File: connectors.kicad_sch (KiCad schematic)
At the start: 10 parts, among them J1 USB-C_DX07S024JJ2, J2 PCIe_x4_Conn_EdgeMount, J3 Molex_Nano-Fit-1053xx_xx02-ho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

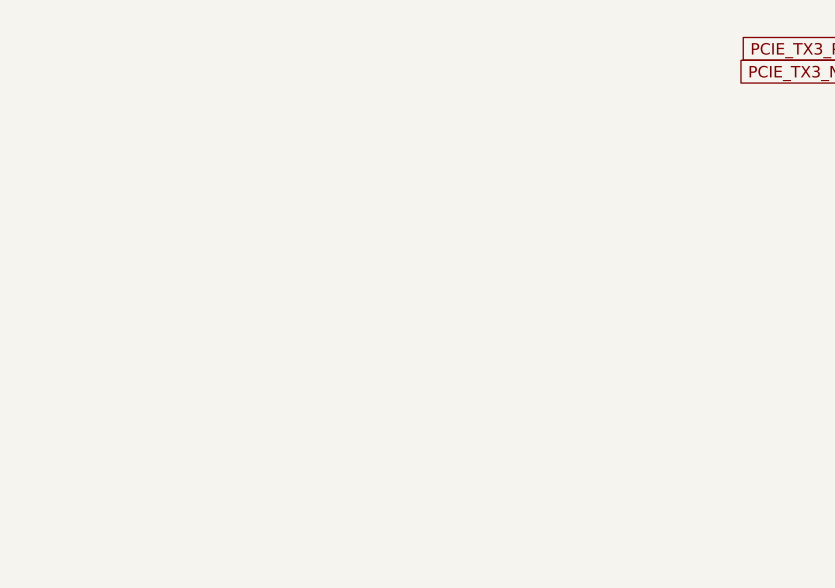
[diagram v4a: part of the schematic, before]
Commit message: Fixed all DRC errors and warnings, finished designators' placement
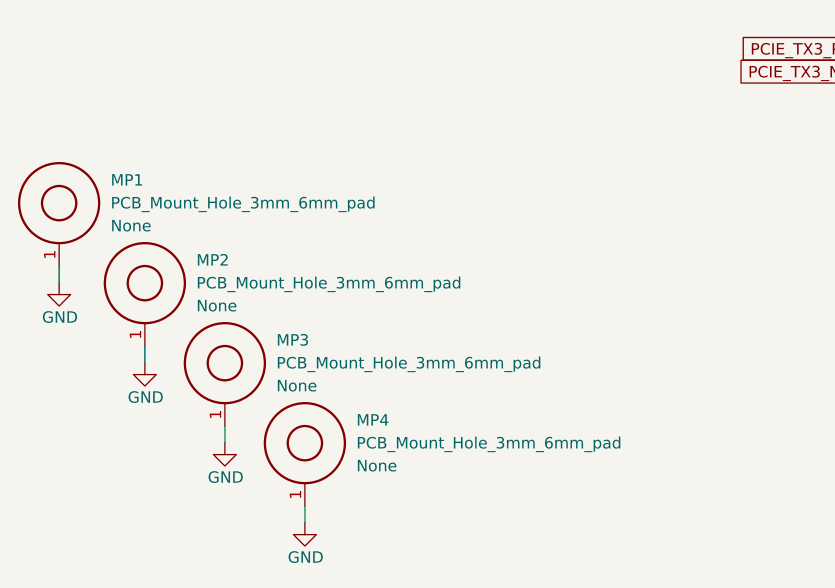
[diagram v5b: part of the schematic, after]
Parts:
- added MP1, MP2, MP3, MP4: PCB_Mount_Hole_3mm_6mm_pad, antmicro-footprints:mounting-hole-3.2mm, symbol antmicroMechanicalParts:PCB_Mount_Hole_3mm_6mm_pad
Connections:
- net GND: now also MP1.1, MP2.1, MP3.1, MP4.1
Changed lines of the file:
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@@
+    (stroke (width 0) (type default) (color 0 0 0 0))
+  )
+  (wire (pts (xy 62.865 383.54) (xy 62.865 385.445))
     (stroke (width 0) (type default) (color 0 0 0 0))
   )
@@
     (stroke (width 0) (type default) (color 0 0 0 0))
   )
+  (wire (pts (xy 45.085 365.76) (xy 45.085 367.665))
+    (stroke (width 0) (type default) (color 0 0 0 0))
+  )
   (wire (pts (xy 161.29 72.39) (xy 170.815 72.39))
     (stroke (width 0) (type default) (color 0 0 0 0))
@@
     (stroke (width 0) (type default) (color 0 0 0 0))
   )
+  (wire (pts (xy 35.56 356.87) (xy 35.56 358.775))
+    (stroke (width 0) (type default) (color 0 0 0 0))
+  )
   (wire (pts (xy 169.545 269.24) (xy 167.64 269.24))
     (stroke (width 0) (type default) (color 0 0 0 0))
@@
   )
   (wire (pts (xy 123.825 281.94) (xy 128.27 281.94))
+    (stroke (width 0) (type default) (color 0 0 0 0))
+  )
+  (wire (pts (xy 53.975 374.65) (xy 53.975 376.555))
     (stroke (width 0) (type default) (color 0 0 0 0))
   )
@@
     )
     (property "Datasheet" "" (id 3) (at 146.685 128.27 0)
+      (effects (font (size 1.27 1.27)) hide)
+    )
+    (pin "1")
+  )
+  (symbol (lib_id "power:GND") (at 53.975 376.555 0) (unit 1)
+    (in_bom yes) (on_board yes)
+    (property "Reference" "#PWR0162" (id 0) (at 53.975 382.905 0)
+      (effects (font (size 1.27 1.27)) hide)
+    )
+    (property "Value" "GND" (id 1) (at 52.07 380.365 0)
+      (effects (font (size 1.27 1.27)) (justify left))
+    )
+    (property "Footprint" "" (id 2) (at 53.975 376.555 0)
+      (effects (font (size 1.27 1.27)) hide)
+    )
+    (property "Datasheet" "" (id 3) (at 53.975 376.555 0)
       (effects (font (size 1.27 1.27)) hide)
     )
@@
     (pin "1")
   )
+  (symbol (lib_id "antmicroMechanicalParts:PCB_Mount_Hole_3mm_6mm_pad") (at 45.085 365.76 90) (unit 1)
+    (in_bom yes) (on_board yes) (fields_autoplaced)
+    (property "Reference" "MP2" (id 0) (at 50.8 356.2349 90)
+      (effects (font (size 1.27 1.27) (thickness 0.15)) (justify right))
+    )
+    (property "Value" "PCB_Mount_Hole_3mm_6mm_pad" (id 1) (at 50.8 358.7749 90)
+      (effects (font (size 1.27 1.27) (thickness 0.15)) (justify right))
+    )
+    (property "Footprint" "antmicro-footprints:mounting-hole-3.2mm" (id 2) (at 52.705 345.44 0)
+      (effects (font (size 1.27 1.27) (thickness 0.15)) (justify left bottom) hide)
+    )
+    (property "Datasheet" "" (id 3) (at 55.245 345.44 0)
+      (effects (font (size 1.27 1.27) (thickness 0.15)) (justify left bottom) hide)
+    )
+    (property "Author" "Antmicro" (id 4) (at 57.785 345.44 0)
+      (effects (font (size 1.27 1.27) (thickness 0.15)) (justify left bottom) hide)
+    )
+    (property "License" "Apache-2.0" (id 5) (at 60.325 345.44 0)
+      (effects (font (size 1.27 1.27) (thickness 0.15)) (justify left bottom) hide)
+    )
+    (property "Manufacturer" "None" (id 6) (at 50.8 361.3149 90)
+      (effects (font (size 1.27 1.27)) (justify right))
+    )
+    (pin "1")
+  )
   (symbol (lib_id "power:GND") (at 181.61 271.145 0) (unit 1)
     (in_bom yes) (on_board yes)
@@
     (pin "1")
   )
+  (symbol (lib_id "power:GND") (at 45.085 367.665 0) (unit 1)
+    (in_bom yes) (on_board yes)
+    (property "Reference" "#PWR0159" (id 0) (at 45.085 374.015 0)
+      (effects (font (size 1.27 1.27)) hide)
+    )
+    (property "Value" "GND" (id 1) (at 43.18 371.475 0)
+      (effects (font (size 1.27 1.27)) (justify left))
+    )
+    (property "Footprint" "" (id 2) (at 45.085 367.665 0)
+      (effects (font (size 1.27 1.27)) hide)
+    )
+    (property "Datasheet" "" (id 3) (at 45.085 367.665 0)
+      (effects (font (size 1.27 1.27)) hide)
+    )
+    (pin "1")
+  )
+  (symbol (lib_id "power:GND") (at 62.865 385.445 0) (unit 1)
+    (in_bom yes) (on_board yes)
+    (property "Reference" "#PWR0161" (id 0) (at 62.865 391.795 0)
+      (effects (font (size 1.27 1.27)) hide)
+    )
+    (property "Value" "GND" (id 1) (at 60.96 389.255 0)
+      (effects (font (size 1.27 1.27)) (justify left))
+    )
+    (property "Footprint" "" (id 2) (at 62.865 385.445 0)
+      (effects (font (size 1.27 1.27)) hide)
+    )
+    (property "Datasheet" "" (id 3) (at 62.865 385.445 0)
+      (effects (font (size 1.27 1.27)) hide)
+    )
+    (pin "1")
+  )
+  (symbol (lib_id "power:GND") (at 35.56 358.775 0) (unit 1)
+    (in_bom yes) (on_board yes)
+    (property "Reference" "#PWR0160" (id 0) (at 35.56 365.125 0)
+      (effects (font (size 1.27 1.27)) hide)
+    )
+    (property "Value" "GND" (id 1) (at 33.655 362.585 0)
+      (effects (font (size 1.27 1.27)) (justify left))
+    )
+    (property "Footprint" "" (id 2) (at 35.56 358.775 0)
+      (effects (font (size 1.27 1.27)) hide)
+    )
+    (property "Datasheet" "" (id 3) (at 35.56 358.775 0)
+      (effects (font (size 1.27 1.27)) hide)
+    )
+    (pin "1")
+  )
+  (symbol (lib_id "antmicroMechanicalParts:PCB_Mount_Hole_3mm_6mm_pad") (at 62.865 383.54 90) (unit 1)
+    (in_bom yes) (on_board yes) (fields_autoplaced)
+    (property "Reference" "MP4" (id 0) (at 68.58 374.0149 90)
+      (effects (font (size 1.27 1.27) (thickness 0.15)) (justify right))
+    )
+    (property "Value" "PCB_Mount_Hole_3mm_6mm_pad" (id 1) (at 68.58 376.5549 90)
+      (effects (font (size 1.27 1.27) (thickness 0.15)) (justify right))
+    )
+    (property "Footprint" "antmicro-footprints:mounting-hole-3.2mm" (id 2) (at 70.485 363.22 0)
+      (effects (font (size 1.27 1.27) (thickness 0.15)) (justify left bottom) hide)
+    )
+    (property "Datasheet" "" (id 3) (at 73.025 363.22 0)
+      (effects (font (size 1.27 1.27) (thickness 0.15)) (justify left bottom) hide)
+    )
+    (property "Author" "Antmicro" (id 4) (at 75.565 363.22 0)
+      (effects (font (size 1.27 1.27) (thickness 0.15)) (justify left bottom) hide)
+    )
+    (property "License" "Apache-2.0" (id 5) (at 78.105 363.22 0)
+      (effects (font (size 1.27 1.27) (thickness 0.15)) (justify left bottom) hide)
+    )
+    (property "Manufacturer" "None" (id 6) (at 68.58 379.0949 90)
+      (effects (font (size 1.27 1.27)) (justify right))
+    )
+    (pin "1")
+  )
   (symbol (lib_id "power:GND") (at 153.035 195.58 0) (unit 1)
     (in_bom yes) (on_board yes)
@@
     (property "Datasheet" "" (id 3) (at 140.335 128.27 0)
       (effects (font (size 1.27 1.27)) hide)
+    )
+    (pin "1")
+  )
+  (symbol (lib_id "antmicroMechanicalParts:PCB_Mount_Hole_3mm_6mm_pad") (at 35.56 356.87 90) (unit 1)
+    (in_bom yes) (on_board yes) (fields_autoplaced)
+    (property "Reference" "MP1" (id 0) (at 41.275 347.3449 90)
+      (effects (font (size 1.27 1.27) (thickness 0.15)) (justify right))
+    )
+    (property "Value" "PCB_Mount_Hole_3mm_6mm_pad" (id 1) (at 41.275 349.8849 90)
+      (effects (font (size 1.27 1.27) (thickness 0.15)) (justify right))
+    )
+    (property "Footprint" "antmicro-footprints:mounting-hole-3.2mm" (id 2) (at 43.18 336.55 0)
+      (effects (font (size 1.27 1.27) (thickness 0.15)) (justify left bottom) hide)
+    )
+    (property "Datasheet" "" (id 3) (at 45.72 336.55 0)
+      (effects (font (size 1.27 1.27) (thickness 0.15)) (justify left bottom) hide)
+    )
+    (property "Author" "Antmicro" (id 4) (at 48.26 336.55 0)
+      (effects (font (size 1.27 1.27) (thickness 0.15)) (justify left bottom) hide)
+    )
+    (property "License" "Apache-2.0" (id 5) (at 50.8 336.55 0)
+      (effects (font (size 1.27 1.27) (thickness 0.15)) (justify left bottom) hide)
+    )
+    (property "Manufacturer" "None" (id 6) (at 41.275 352.4249 90)
+      (effects (font (size 1.27 1.27)) (justify right))
     )
     (pin "1")
@@
     (pin "2")
   )
+  (symbol (lib_id "antmicroMechanicalParts:PCB_Mount_Hole_3mm_6mm_pad") (at 53.975 374.65 90) (unit 1)
+    (in_bom yes) (on_board yes) (fields_autoplaced)
+    (property "Reference" "MP3" (id 0) (at 59.69 365.1249 90)
+      (effects (font (size 1.27 1.27) (thickness 0.15)) (justify right))
+    )
+    (property "Value" "PCB_Mount_Hole_3mm_6mm_pad" (id 1) (at 59.69 367.6649 90)
+      (effects (font (size 1.27 1.27) (thickness 0.15)) (justify right))
+    )
+    (property "Footprint" "antmicro-footprints:mounting-hole-3.2mm" (id 2) (at 61.595 354.33 0)
+      (effects (font (size 1.27 1.27) (thickness 0.15)) (justify left bottom) hide)
+    )
+    (property "Datasheet" "" (id 3) (at 64.135 354.33 0)
+      (effects (font (size 1.27 1.27) (thickness 0.15)) (justify left bottom) hide)
+    )
+    (property "Author" "Antmicro" (id 4) (at 66.675 354.33 0)
+      (effects (font (size 1.27 1.27) (thickness 0.15)) (justify left bottom) hide)
+    )
+    (property "License" "Apache-2.0" (id 5) (at 69.215 354.33 0)
+      (effects (font (size 1.27 1.27) (thickness 0.15)) (justify left bottom) hide)
+    )
+    (property "Manufacturer" "None" (id 6) (at 59.69 370.2049 90)
+      (effects (font (size 1.27 1.27)) (justify right))
+    )
+    (pin "1")
+  )
   (symbol (lib_id "antmicroCapacitorsmisc:C_10u_0805_35V") (at 120.65 269.24 90) (unit 1)

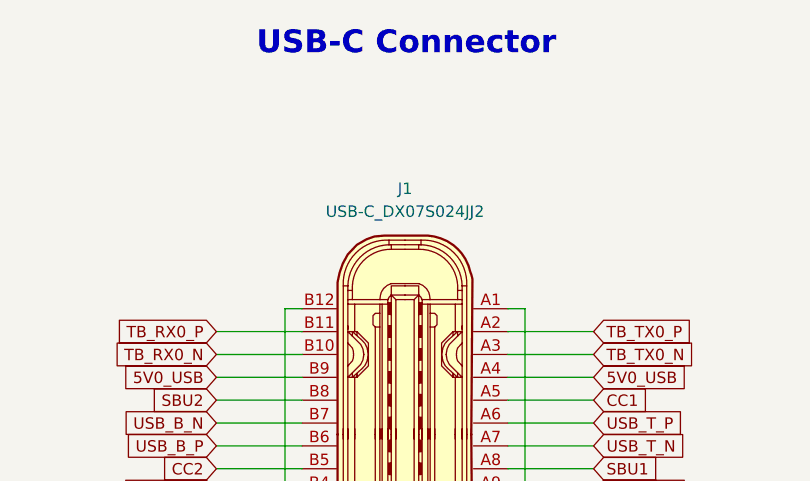
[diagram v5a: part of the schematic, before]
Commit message: Updated J1 footprint and symbol after small tweaks in library
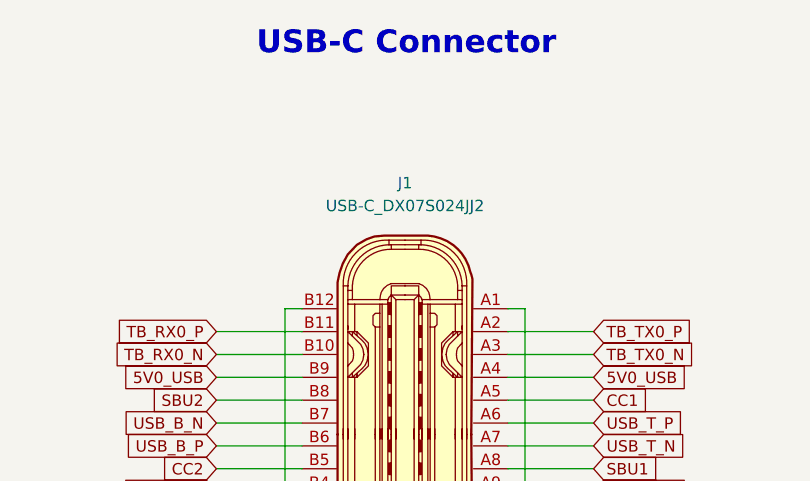
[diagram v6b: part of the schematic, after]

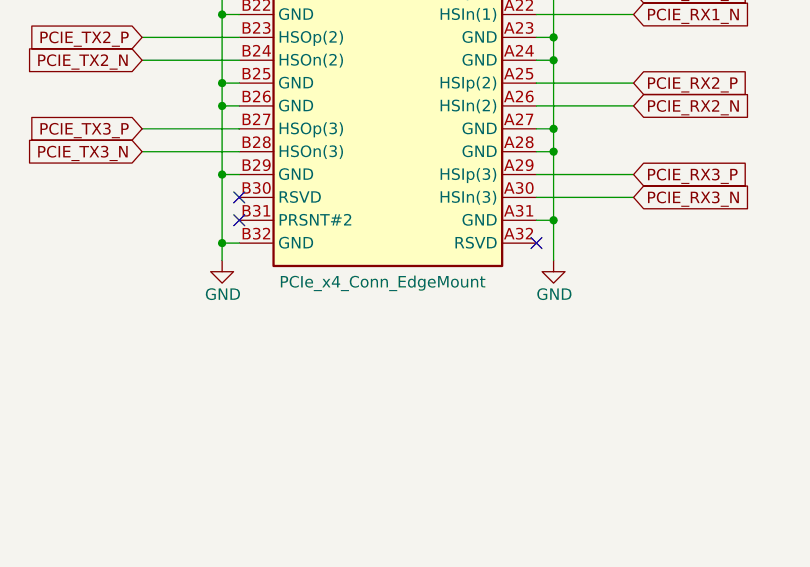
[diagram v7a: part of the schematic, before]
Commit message: Changed PCIe connector to TE Connectivity 6-1734857-5
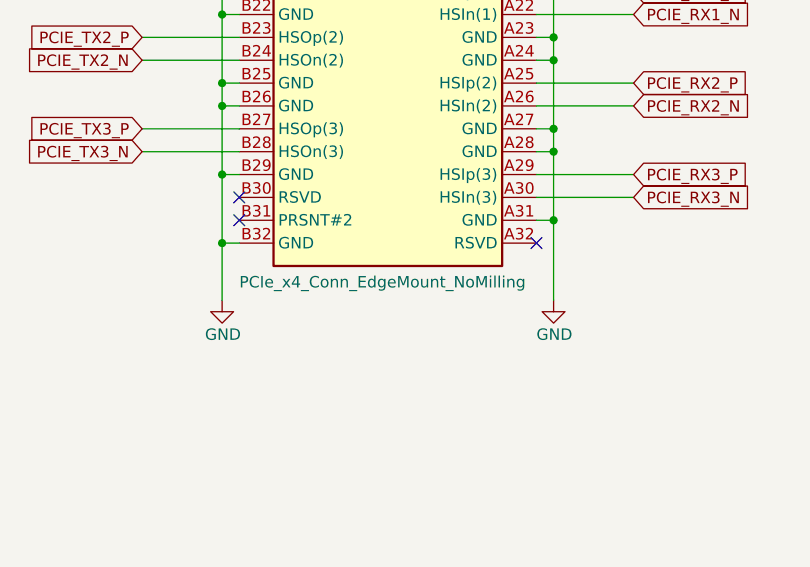
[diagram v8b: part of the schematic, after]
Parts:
- J2: value PCIe_x4_Conn_EdgeMount -> PCIe_x4_Conn_EdgeMount_NoMilling; footprint antmicro-footprints:PCIE_PCIE-064-02-X-D-EMSX -> antmicro-footprints:PCIE_TE_6-1734857-5; symbol antmicroPciConnectors:PCIe_x4_Conn_EdgeMount -> antmicroPciConnectors:PCIe_x4_Conn_EdgeMount_NoMilling; Author (none) -> Antmicro; License Apache-2.0 License -> Apache-2.0; MPN PCIE-064-02-X-D-EMSX -> 6-1734857-5; Manufacturer Samtec -> TE Connectivity
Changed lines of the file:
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@@
     (stroke (width 0) (type default) (color 0 0 0 0))
   )
-  (wire (pts (xy 169.545 342.9) (xy 169.545 347.345))
+  (wire (pts (xy 169.545 342.9) (xy 169.545 351.79))
     (stroke (width 0) (type default) (color 0 0 0 0))
   )
@@
     (stroke (width 0) (type default) (color 0 0 0 0))
   )
-  (wire (pts (xy 132.715 345.44) (xy 132.715 347.345))
+  (wire (pts (xy 132.715 345.44) (xy 132.715 351.79))
     (stroke (width 0) (type default) (color 0 0 0 0))
   )
@@
     (pin "2")
   )
-  (symbol (lib_id "power:GND") (at 132.715 347.345 0) (unit 1)
-    (in_bom yes) (on_board yes)
-    (property "Reference" "#PWR02" (id 0) (at 132.715 353.695 0)
-      (effects (font (size 1.27 1.27)) hide)
-    )
-    (property "Value" "GND" (id 1) (at 130.81 351.155 0)
-      (effects (font (size 1.27 1.27)) (justify left))
-    )
-    (property "Footprint" "" (id 2) (at 132.715 347.345 0)
-      (effects (font (size 1.27 1.27)) hide)
-    )
-    (property "Datasheet" "" (id 3) (at 132.715 347.345 0)
+  (symbol (lib_id "power:GND") (at 132.715 351.79 0) (unit 1)
+    (in_bom yes) (on_board yes)
+    (property "Reference" "#PWR02" (id 0) (at 132.715 358.14 0)
+      (effects (font (size 1.27 1.27)) hide)
+    )
+    (property "Value" "GND" (id 1) (at 130.81 355.6 0)
+      (effects (font (size 1.27 1.27)) (justify left))
+    )
+    (property "Footprint" "" (id 2) (at 132.715 351.79 0)
+      (effects (font (size 1.27 1.27)) hide)
+    )
+    (property "Datasheet" "" (id 3) (at 132.715 351.79 0)
       (effects (font (size 1.27 1.27)) hide)
     )
@@
     (pin "SH")
   )
-  (symbol (lib_id "antmicroPciConnectors:PCIe_x4_Conn_EdgeMount") (at 134.62 264.16 0) (unit 1)
+  (symbol (lib_id "antmicroPciConnectors:PCIe_x4_Conn_EdgeMount_NoMilling") (at 134.62 264.16 0) (unit 1)
     (in_bom yes) (on_board yes)
     (property "Reference" "J2" (id 0) (at 139.7 260.35 0)
       (effects (font (size 1.27 1.27) (thickness 0.15)))
     )
-    (property "Value" "PCIe_x4_Conn_EdgeMount" (id 1) (at 139.065 350.52 0)
+    (property "Value" "PCIe_x4_Conn_EdgeMount_NoMilling" (id 1) (at 134.62 350.52 0)
       (effects (font (size 1.27 1.27) (thickness 0.15)) (justify left bottom))
     )
-    (property "Footprint" "antmicro-footprints:PCIE_PCIE-064-02-X-D-EMSX" (id 2) (at 182.88 271.78 0)
-      (effects (font (size 1.27 1.27) (thickness 0.15)) (justify left bottom) hide)
-    )
-    (property "Datasheet" "http://www.farnell.com/datasheets/2048385.pdf?_ga=2.224413790.550525831.1572511829-156563690.1566371002&_gac=1.194368863.1572511829.Cj0KCQjwjOrtBRCcARIsAEq4rW4MDAz553xUSGW1I2S05saoepO8CZq5otyVO6_gct6IiE-jnZiday4aAmKSEALw_wcB" (id 3) (at 182.88 274.32 0)
-      (effects (font (size 1.27 1.27) (thickness 0.15)) (justify left bottom) hide)
-    )
-    (property "MPN" "PCIE-064-02-X-D-EMSX" (id 4) (at 182.88 276.86 0)
-      (effects (font (size 1.27 1.27) (thickness 0.15)) (justify left bottom) hide)
-    )
-    (property "Manufacturer" "Samtec" (id 5) (at 182.88 279.4 0)
+    (property "Footprint" "antmicro-footprints:PCIE_TE_6-1734857-5" (id 2) (at 182.88 271.78 0)
+      (effects (font (size 1.27 1.27) (thickness 0.15)) (justify left bottom) hide)
+    )
+    (property "Datasheet" "https://www.te.com/commerce/DocumentDelivery/DDEController?Action=showdoc&DocId=Customer+Drawing%7F1734857%7FC%7Fpdf%7FEnglish%7FENG_CD_1734857_C.pdf%7F6-1734857-5" (id 3) (at 182.88 274.32 0)
+      (effects (font (size 1.27 1.27) (thickness 0.15)) (justify left bottom) hide)
+    )
+    (property "MPN" "6-1734857-5" (id 4) (at 182.88 276.86 0)
+      (effects (font (size 1.27 1.27) (thickness 0.15)) (justify left bottom) hide)
+    )
+    (property "Manufacturer" "TE Connectivity" (id 5) (at 182.88 279.4 0)
       (effects (font (size 1.27 1.27) (thickness 0.15)) (justify left bottom) hide)
     )
@@
       (effects (font (size 1.27 1.27) (thickness 0.15)) (justify left bottom) hide)
     )
-    (property "License" "Apache-2.0 License" (id 7) (at 182.88 284.48 0)
+    (property "License" "Apache-2.0" (id 7) (at 182.88 284.48 0)
+      (effects (font (size 1.27 1.27) (thickness 0.15)) (justify left bottom) hide)
+    )
+    (property "Author" "Antmicro" (id 8) (at 182.88 281.94 0)
       (effects (font (size 1.27 1.27) (thickness 0.15)) (justify left bottom) hide)
     )
@@
     (pin "B9")
   )
-  (symbol (lib_id "power:GND") (at 169.545 347.345 0) (unit 1)
-    (in_bom yes) (on_board yes)
-    (property "Reference" "#PWR010" (id 0) (at 169.545 353.695 0)
-      (effects (font (size 1.27 1.27)) hide)
-    )
-    (property "Value" "GND" (id 1) (at 167.64 351.155 0)
-      (effects (font (size 1.27 1.27)) (justify left))
-    )
-    (property "Footprint" "" (id 2) (at 169.545 347.345 0)
-      (effects (font (size 1.27 1.27)) hide)
-    )
-    (property "Datasheet" "" (id 3) (at 169.545 347.345 0)
-      (effects (font (size 1.27 1.27)) hide)
-    )
+  (symbol (lib_id "power:GND") (at 169.545 351.79 0) (unit 1)
+    (in_bom yes) (on_board yes)
+    (property "Reference" "#PWR010" (id 0) (at 169.545 358.14 0)
+      (effects (font (size 1.27 1.27)) hide)
+    )
+    (property "Value" "GND" (id 1) (at 167.64 355.6 0)
+      (effects (font (size 1.27 1.27)) (justify left))
+    )
+    (property "Footprint" "" (id 2) (at 169.545 351.79 0)
+      (effects (font (size 1.27 1.27)) hide)
+    )
+    (property "Datasheet" "" (id 3) (at 169.545 351.79 0)
+      (effects (font (size 1.27 1.27)) hide)
+    )
